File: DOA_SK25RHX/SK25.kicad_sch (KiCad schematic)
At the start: 41 parts, among them J1 Imput-, J2 Input+, J3 V+, J4 Output, J5 V-, J6 GND, Q1 BC560C, Q10 BD140, Q2 KSA992, Q3 KSA992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

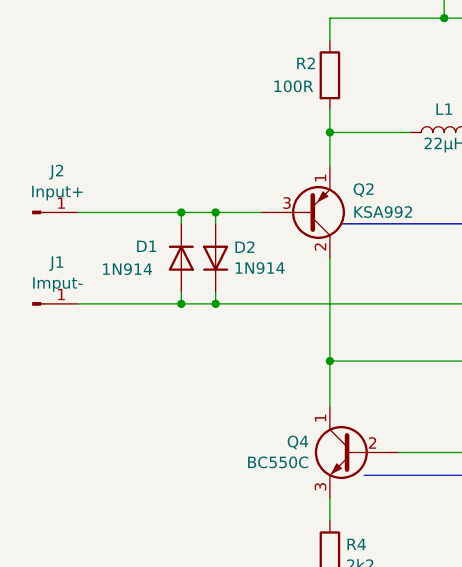
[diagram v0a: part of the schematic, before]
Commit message: completed routing, except diose pads
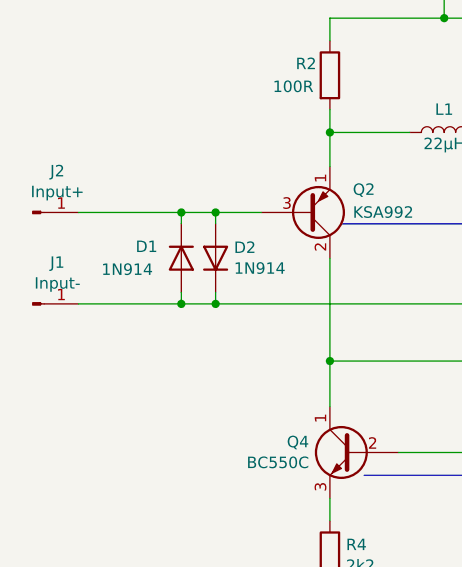
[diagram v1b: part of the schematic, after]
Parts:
- J1: value Imput- -> Input-
- Q10, Q9: footprint Package_TO_SOT_THT:TO-220-3_Horizontal_TabDown -> TAC:to225_std
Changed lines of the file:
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@@
       (effects (font (size 1.27 1.27)) (justify left))
     )
-    (property "Footprint" "Package_TO_SOT_THT:TO-220-3_Horizontal_TabDown" (id 2) (at 193.04 104.14 0)
+    (property "Footprint" "TAC:to225_std" (id 2) (at 193.04 104.14 0)
       (effects (font (size 1.27 1.27)) hide)
     )
@@
       (effects (font (size 1.27 1.27)) (justify left))
     )
-    (property "Footprint" "Package_TO_SOT_THT:TO-220-3_Horizontal_TabDown" (id 2) (at 193.04 60.96 0)
+    (property "Footprint" "TAC:to225_std" (id 2) (at 193.04 60.96 0)
       (effects (font (size 1.27 1.27)) hide)
     )
@@
     (in_bom yes) (on_board yes)
     (property "Reference" "J1" (id 0) (at 45.9232 90.6526 0))
-    (property "Value" "Imput-" (id 1) (at 45.9232 92.964 0))
+    (property "Value" "Input-" (id 1) (at 45.9232 92.964 0))
     (property "Footprint" "Connector_Pin:Pin_D1.1mm_L8.5mm_W2.5mm_FlatFork" (id 2) (at 43.18 95.25 0)
       (effects (font (size 1.27 1.27)) hide)
@@
     )
     (path "/00000000-0000-0000-0000-000062fae296"
-      (reference "J1") (unit 1) (value "Imput-") (footprint "Connector_Pin:Pin_D1.1mm_L8.5mm_W2.5mm_FlatFork")
+      (reference "J1") (unit 1) (value "Input-") (footprint "Connector_Pin:Pin_D1.1mm_L8.5mm_W2.5mm_FlatFork")
     )
     (path "/00000000-0000-0000-0000-000062faa65b"
@@
     )
     (path "/00000000-0000-0000-0000-00005fe3c93a"
-      (reference "Q9") (unit 1) (value "BD139") (footprint "Package_TO_SOT_THT:TO-220-3_Horizontal_TabDown")
+      (reference "Q9") (unit 1) (value "BD139") (footprint "TAC:to225_std")
     )
     (path "/00000000-0000-0000-0000-00005fe396bc"
-      (reference "Q10") (unit 1) (value "BD140") (footprint "Package_TO_SOT_THT:TO-220-3_Horizontal_TabDown")
+      (reference "Q10") (unit 1) (value "BD140") (footprint "TAC:to225_std")
     )
     (path "/00000000-0000-0000-0000-00005fdeb6a1"

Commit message: modified BJT footprints
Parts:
- Q1, Q2, Q3, Q4, Q5, Q6, Q7, Q8: footprint Package_TO_SOT_THT:TO-92 -> TAC:TO-92
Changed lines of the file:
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@@
       (effects (font (size 1.27 1.27)) (justify left))
     )
-    (property "Footprint" "Package_TO_SOT_THT:TO-92" (id 2) (at 78.74 87.63 0)
+    (property "Footprint" "TAC:TO-92" (id 2) (at 78.74 87.63 0)
       (effects (font (size 1.27 1.27)) hide)
     )
@@
       (effects (font (size 1.27 1.27)) (justify left))
     )
-    (property "Footprint" "Package_TO_SOT_THT:TO-92" (id 2) (at 99.06 87.63 0)
+    (property "Footprint" "TAC:TO-92" (id 2) (at 99.06 87.63 0)
       (effects (font (size 1.27 1.27)) hide)
     )
@@
       (effects (font (size 1.27 1.27)) (justify left))
     )
-    (property "Footprint" "Package_TO_SOT_THT:TO-92" (id 2) (at 86.36 58.42 0)
+    (property "Footprint" "TAC:TO-92" (id 2) (at 86.36 58.42 0)
       (effects (font (size 1.27 1.27)) hide)
     )
@@
       (effects (font (size 1.27 1.27)) (justify left))
     )
-    (property "Footprint" "Package_TO_SOT_THT:TO-92" (id 2) (at 104.14 109.22 0)
+    (property "Footprint" "TAC:TO-92" (id 2) (at 104.14 109.22 0)
       (effects (font (size 1.27 1.27)) hide)
     )
@@
       (effects (font (size 1.27 1.27)) (justify left))
     )
-    (property "Footprint" "Package_TO_SOT_THT:TO-92" (id 2) (at 73.66 109.22 0)
+    (property "Footprint" "TAC:TO-92" (id 2) (at 73.66 109.22 0)
       (effects (font (size 1.27 1.27)) hide)
     )
@@
       (effects (font (size 1.27 1.27)) (justify left))
     )
-    (property "Footprint" "Package_TO_SOT_THT:TO-92" (id 2) (at 124.46 109.22 0)
+    (property "Footprint" "TAC:TO-92" (id 2) (at 124.46 109.22 0)
       (effects (font (size 1.27 1.27)) hide)
     )
@@
       (effects (font (size 1.27 1.27)) (justify left))
     )
-    (property "Footprint" "Package_TO_SOT_THT:TO-92" (id 2) (at 167.64 116.84 0)
+    (property "Footprint" "TAC:TO-92" (id 2) (at 167.64 116.84 0)
       (effects (font (size 1.27 1.27)) hide)
     )
@@
       (effects (font (size 1.27 1.27)) (justify left))
     )
-    (property "Footprint" "Package_TO_SOT_THT:TO-92" (id 2) (at 167.64 58.42 0)
+    (property "Footprint" "TAC:TO-92" (id 2) (at 167.64 58.42 0)
       (effects (font (size 1.27 1.27)) hide)
     )
@@
     )
     (path "/00000000-0000-0000-0000-00005fdea503"
-      (reference "Q1") (unit 1) (value "BC560C") (footprint "Package_TO_SOT_THT:TO-92")
+      (reference "Q1") (unit 1) (value "BC560C") (footprint "TAC:TO-92")
     )
     (path "/00000000-0000-0000-0000-00005fde49ff"
-      (reference "Q2") (unit 1) (value "KSA992") (footprint "Package_TO_SOT_THT:TO-92")
+      (reference "Q2") (unit 1) (value "KSA992") (footprint "TAC:TO-92")
     )
     (path "/00000000-0000-0000-0000-00005fde6888"
-      (reference "Q3") (unit 1) (value "KSA992") (footprint "Package_TO_SOT_THT:TO-92")
+      (reference "Q3") (unit 1) (value "KSA992") (footprint "TAC:TO-92")
     )
     (path "/00000000-0000-0000-0000-00005fdee020"
-      (reference "Q4") (unit 1) (value "BC550C") (footprint "Package_TO_SOT_THT:TO-92")
+      (reference "Q4") (unit 1) (value "BC550C") (footprint "TAC:TO-92")
     )
     (path "/00000000-0000-0000-0000-00005fdecfb4"
-      (reference "Q5") (unit 1) (value "BC550C") (footprint "Package_TO_SOT_THT:TO-92")
+      (reference "Q5") (unit 1) (value "BC550C") (footprint "TAC:TO-92")
     )
     (path "/00000000-0000-0000-0000-00005fdfd85f"
-      (reference "Q6") (unit 1) (value "BC550C") (footprint "Package_TO_SOT_THT:TO-92")
+      (reference "Q6") (unit 1) (value "BC550C") (footprint "TAC:TO-92")
     )
     (path "/00000000-0000-0000-0000-00005fe2b139"
-      (reference "Q7") (unit 1) (value "BC556C") (footprint "Package_TO_SOT_THT:TO-92")
+      (reference "Q7") (unit 1) (value "BC556C") (footprint "TAC:TO-92")
     )
     (path "/00000000-0000-0000-0000-00005fe09e9c"
-      (reference "Q8") (unit 1) (value "BC546C") (footprint "Package_TO_SOT_THT:TO-92")
+      (reference "Q8") (unit 1) (value "BC546C") (footprint "TAC:TO-92")
     )
     (path "/00000000-0000-0000-0000-00005fe3c93a"
